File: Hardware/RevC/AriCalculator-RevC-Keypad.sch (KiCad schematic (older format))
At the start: 30 parts

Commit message: work in progress
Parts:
- added KEY_E5, KEY_F5, KEY_G0, KEY_G1, KEY_G2, KEY_G3, KEY_G4, KEY_G5: KEY, ~, symbol KEY
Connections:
- net KEYPAD_COL_0: no longer KEY_E0.2, KEY_F0.2, KEY_F0.4, KEY_F0.6
- net KEYPAD_COL_1: no longer KEY_D1.2, KEY_E1.2, KEY_E1.4, KEY_E1.6, KEY_F1.2, KEY_F1.4, KEY_F1.6
- net KEYPAD_COL_2: now also KEY_G2.2, KEY_G2.4, KEY_G2.6
- net KEYPAD_COL_3: no longer KEY_A3.2, KEY_B3.2, KEY_B3.4, KEY_B3.6, KEY_C3.2, KEY_C3.4, KEY_C3.6, KEY_D3.2, KEY_D3.4, KEY_D3.6, KEY_E3.2, KEY_E3.4, KEY_E3.6, KEY_F3.2, KEY_F3.4, KEY_F3.6
- net KEYPAD_COL_4: now also KEY_G4.2, KEY_G4.4, KEY_G4.6
- net KEYPAD_ROW_E: now also KEY_E5.1, KEY_E5.3, KEY_E5.5
- net KEYPAD_ROW_F: now also KEY_F5.1, KEY_F5.3, KEY_F5.5
- new net: KEY_A3.2, KEY_B3.2, KEY_B3.4, KEY_B3.6, KEY_C3.2, KEY_C3.4, KEY_C3.6, KEY_D3.2, KEY_D3.4, KEY_D3.6, KEY_E3.2, KEY_E3.4, KEY_E3.6, KEY_F3.2, KEY_F3.4, KEY_F3.6, KEY_G3.2, KEY_G3.4, KEY_G3.6
- new net: KEY_E1.2, KEY_E1.4, KEY_E1.6, KEY_F1.2, KEY_F1.4, KEY_F1.6, KEY_G1.2, KEY_G1.4, KEY_G1.6
- new net: KEY_F0.2, KEY_F0.4, KEY_F0.6, KEY_G0.2, KEY_G0.4, KEY_G0.6
- new net KEYPAD_COL_5: KEY_E5.2, KEY_E5.4, KEY_E5.6, KEY_F5.2, KEY_F5.4, KEY_F5.6, KEY_G5.2, KEY_G5.4, KEY_G5.6
- new net KEYPAD_ROW_G: KEY_G0.1, KEY_G0.3, KEY_G0.5, KEY_G1.1, KEY_G1.3, KEY_G1.5, KEY_G2.1, KEY_G2.3, KEY_G2.5, KEY_G3.1, KEY_G3.3, KEY_G3.5, KEY_G4.1, KEY_G4.3, KEY_G4.5, KEY_G5.1, KEY_G5.3, KEY_G5.5

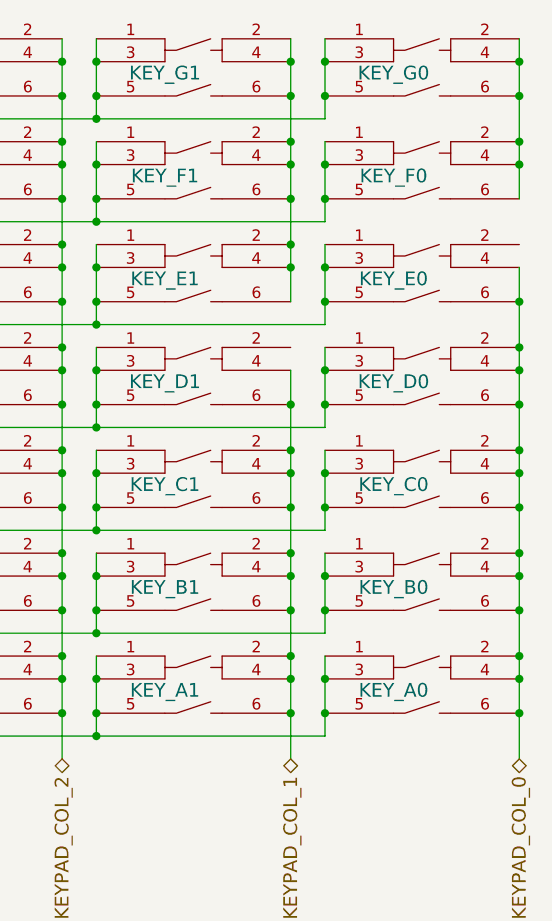
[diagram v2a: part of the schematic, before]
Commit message: started RevC layout
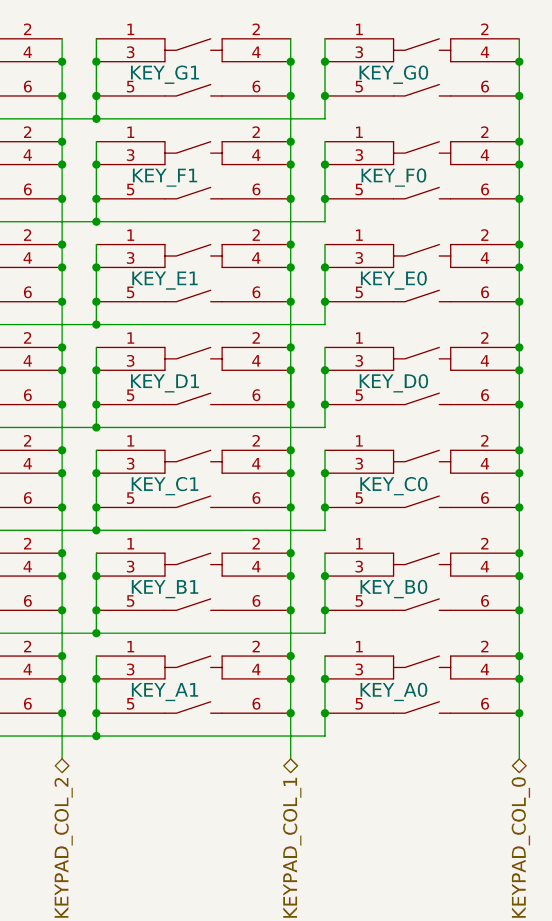
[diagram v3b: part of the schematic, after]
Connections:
- net KEYPAD_COL_0: now also KEY_E0.2, KEY_F0.2, KEY_F0.4, KEY_F0.6, KEY_G0.2, KEY_G0.4, KEY_G0.6
- net KEYPAD_COL_1: now also KEY_D1.2, KEY_E1.2, KEY_E1.4, KEY_E1.6, KEY_F1.2, KEY_F1.4, KEY_F1.6, KEY_G1.2, KEY_G1.4, KEY_G1.6
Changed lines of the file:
@@
 Connection ~ 5400 3650
 Wire Wire Line
-	6400 700  6400 1850
+	6400 700  6400 3850
 Connection ~ 6400 800
 Connection ~ 6400 950
@@
 Connection ~ 6400 1250
 Connection ~ 6400 1400
-Wire Wire Line
-	6400 2150 6400 3850
 Connection ~ 6400 2300
 Connection ~ 6400 2500
@@
 Connection ~ 6400 1600
 Wire Wire Line
-	7400 700  7400 1400
+	7400 700  7400 3850
 Connection ~ 7400 800
 Connection ~ 7400 950
 Connection ~ 7400 1150
 Connection ~ 7400 1250
-Wire Wire Line
-	7400 1700 7400 3850
 Connection ~ 7400 1850
 Connection ~ 7400 2050
@@
 Connection ~ 6400 3400
 Connection ~ 6400 3650
+Connection ~ 6400 1850
+Connection ~ 6400 2150
+Connection ~ 6400 2050
+Wire Wire Line
+	6400 2150 6400 2300
+Connection ~ 7400 1700
+Connection ~ 7400 1400
+Connection ~ 7400 1600
 $EndSCHEMATC

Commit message: work in progress
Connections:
- net KEYPAD_COL_3: now also KEY_A3.2, KEY_B3.2, KEY_B3.4, KEY_B3.6, KEY_C3.2, KEY_C3.4, KEY_C3.6, KEY_D3.2, KEY_D3.4, KEY_D3.6, KEY_E3.2, KEY_E3.4, KEY_E3.6, KEY_F3.2, KEY_F3.4, KEY_F3.6, KEY_G3.2, KEY_G3.4, KEY_G3.6
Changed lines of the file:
@@
 Sheet 3 6
 Title ""
-Date "4 nov 2014"
+Date "5 nov 2014"
 Rev "RevC"
 Comp "Dirk Heisswolf"
@@
 Connection ~ 3400 2150
 Wire Wire Line
-	4400 700  4400 3400
+	4400 700  4400 3850
 Connection ~ 4400 800
 Connection ~ 4400 950
@@
 Connection ~ 3400 3650
 Connection ~ 4400 3200
-Wire Wire Line
-	4400 3500 4400 3850
 Connection ~ 4400 3650
 Connection ~ 5400 3200
@@
 Connection ~ 7400 1400
 Connection ~ 7400 1600
+Connection ~ 4400 3500
+Connection ~ 4400 3400
 $EndSCHEMATC
